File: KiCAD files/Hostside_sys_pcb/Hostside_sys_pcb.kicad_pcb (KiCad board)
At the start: 2 copper layers, 45.7 x 78.7 mm, 8 parts, among them U1 L7805, U2 Raspberry Pi Pico

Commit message: host side kicad files added and updated
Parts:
- U2: value Raspberry Pi Pico -> Pico
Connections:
- BT1 pad 2: /GND -> GND
- C1 pad 2: /GND -> GND
- C2 pad 2: /GND -> GND
- MPU6050 pad 2: /GND_MPU -> GND
- RF433Tx1 pad 1: /GND -> GND
- U1 pad 2: /GND -> GND
- U2 pad 16: unconnected-(U2-Pad16) -> /SDA
- U2 pad 17: unconnected-(U2-Pad17) -> /SCL
- U2 pad 26: /SDA -> unconnected-(U2-Pad26)
- U2 pad 27: /SCL -> unconnected-(U2-Pad27)
- U2 pad 28: /GND -> GND
- U2 pad 38: /GND_MPU -> GND
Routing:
- net /SCL: track 36.8 -> 22.3 mm
- net /SDA: track 42.2 -> 29.9 mm
- net /Data: track 21.2 -> 14.3 mm
- net /GND_MPU: track 6.28 -> 0.00 mm
- net /VCC_3.3: track 53.9 -> 58.3 mm
- net /GND: track 3.83 -> 0.00 mm
- added copper zone on B.Cu, net GND
- removed copper zone on B.Cu, net /GND

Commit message: Hostside kicad files updated and added
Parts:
- C1, C2: footprint Capacitor_THT:CP_Radial_D5.0mm_P2.00mm -> Capacitor_THT:CP_Radial_D5.0mm_P2.50mm
- D1: footprint Diode_THT:D_A-405_P7.62mm_Horizontal -> Diode_THT:D_A-405_P2.54mm_Vertical_KathodeUp
- moved D1 3.13 mm to (95.2, 52.1)
- moved MPU6050 1.60 mm to (64.9, 107.1)
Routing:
- net Net-(D1-Pad1): track 9.52 -> 11.8 mm
- net /SDA: track 29.9 -> 31.7 mm
- net /VCC_3.3: track 58.3 -> 56.8 mm
- net /Vin_5V: track 64.7 -> 66.1 mm
- net /SCL: track 22.3 -> 23.5 mm

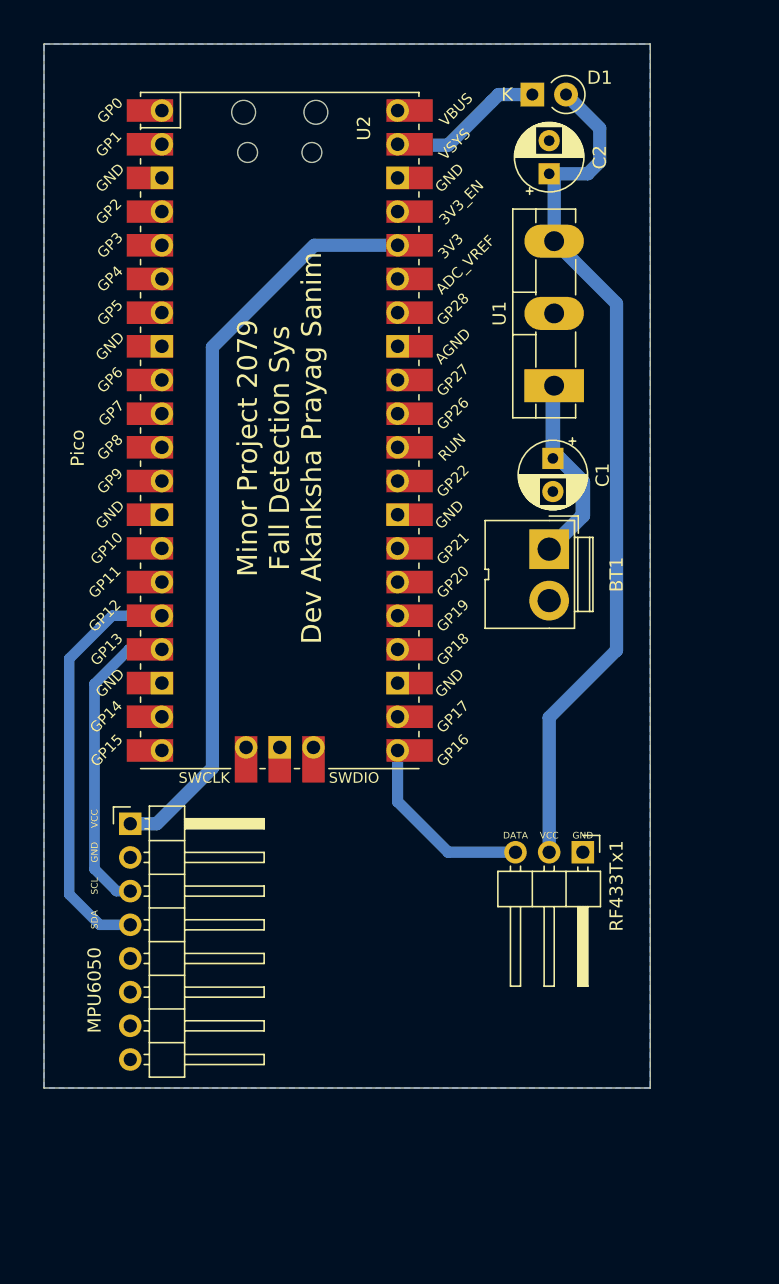
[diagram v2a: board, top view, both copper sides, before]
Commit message: clearance updated in hostside pcb
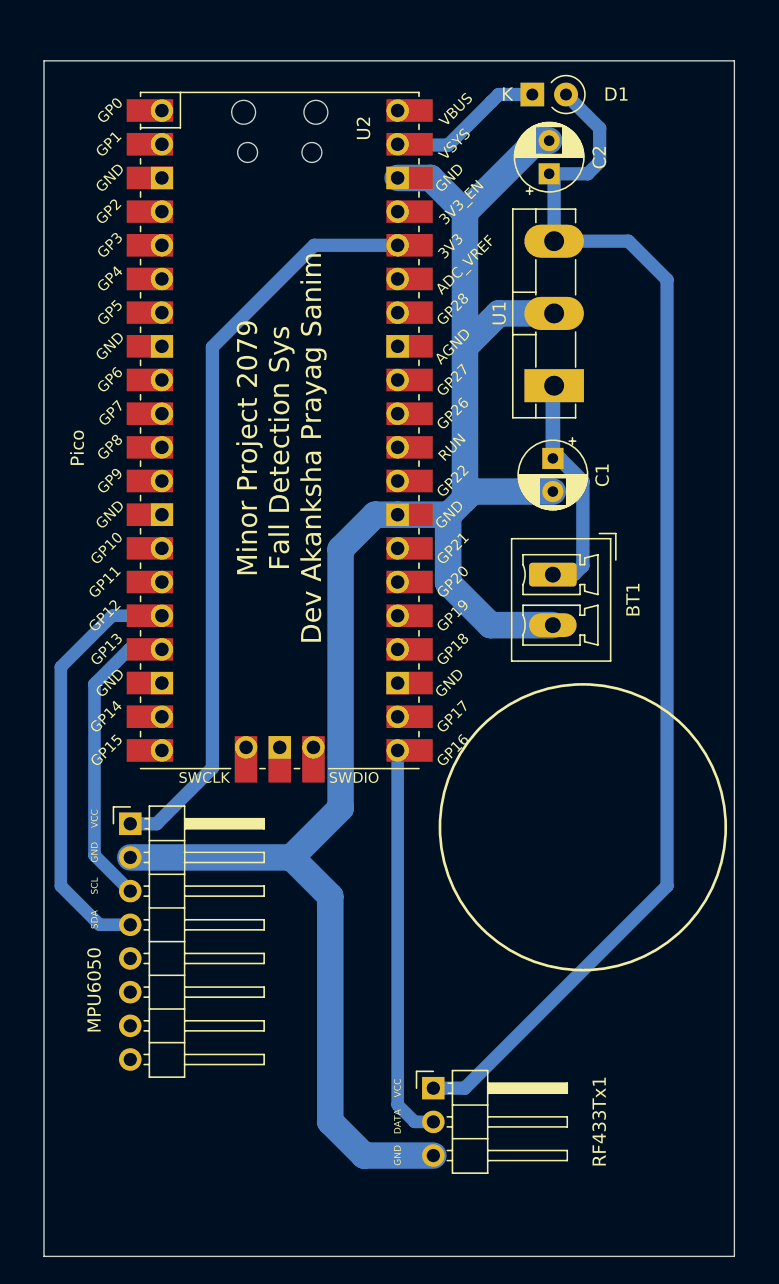
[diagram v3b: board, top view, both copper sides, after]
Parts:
- BT1: footprint Connector:JWT_A3963_1x02_P3.96mm_Vertical -> Connector_Phoenix_MC:PhoenixContact_MCV_1,5_2-G-3.81_1x02_P3.81mm_Vertical
- moved RF433Tx1 21.1 mm to (87.8, 127.0), turned to 0 degrees
- moved BT1 1.94 mm to (96.8, 88.3)
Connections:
- RF433Tx1 pad 1: GND -> /Vin_5V
- RF433Tx1 pad 2: /Vin_5V -> /Data
- RF433Tx1 pad 3: /Data -> GND
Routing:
- net GND: track 0.00 -> 143.2 mm
- net /Vin_5V: track 66.1 -> 95.3 mm
- net /Data: track 14.3 -> 30.0 mm
- net Net-(BT1-Pad1): track 14.6 -> 17.4 mm
- net /SCL: track 23.5 -> 22.9 mm
- net /SDA: track 31.7 -> 32.2 mm
- removed copper zone on B.Cu, net GND
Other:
- board size 45.7 x 78.7 mm -> 52.1 x 90.2 mm

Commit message: Use case and Sequence diagram added
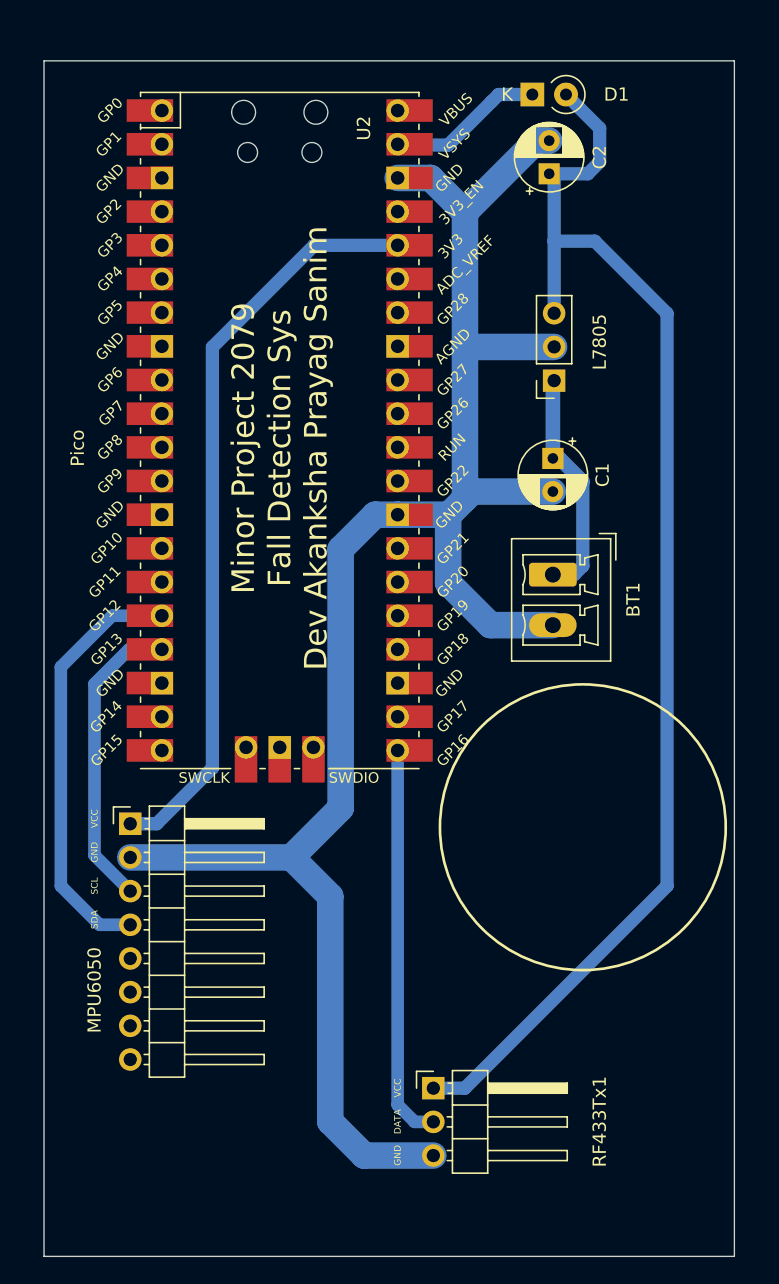
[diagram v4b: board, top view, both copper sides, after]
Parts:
- U1: footprint Package_TO_SOT_THT:TO-3P-3_Vertical -> Connector_PinSocket_2.54mm:PinSocket_1x03_P2.54mm_Vertical
- moved U1 0.39 mm to (96.9, 73.6), turned to 180 degrees
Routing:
- net /Vin_5V: track 95.3 -> 99.3 mm
- net GND: track 143.2 -> 142.1 mm
- net Net-(BT1-Pad1): track 17.4 -> 17.9 mm

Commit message: Host side pcb updates
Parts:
- removed RF433Tx1: Conn_01x03_Female, Connector_PinHeader_2.54mm:PinHeader_1x03_P2.54mm_Horizontal
- added HC-05 Bluetooth: Conn_01x06_Female, Connector_PinHeader_2.54mm:PinHeader_1x06_P2.54mm_Vertical, F.Cu at (87.9, 128.3)
- moved C2 3.20 mm to (97.8, 61.0)
- moved D1 1.32 mm to (95.6, 53.3)
- renumbered U2 to U1, U1 to U2
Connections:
- U1 pad 21: /Data -> /tx
- U1 pad 22: unconnected-(U2-Pad22) -> /rx
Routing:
- net /Data: track 30.0 -> 0.00 mm
- net /rx: track 0.00 -> 27.9 mm
- net /tx: track 0.00 -> 18.7 mm
- net GND: track 142.1 -> 131.7 mm
- net /SCL: track 22.9 -> 23.6 mm
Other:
- board size 52.1 x 90.2 mm -> 53.3 x 81.3 mm
- board text added: "+"
- board text added: "-"
- board text added: "C1:C2=1:10"
- board text added: "EN"
- board text added: "MPU6050"
- board text added: "RX"
- board text added: "TX"
- board text removed: "DATA"

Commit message: files merge
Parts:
- moved HC-05 Bluetooth 6.42 mm to (88.9, 134.6)
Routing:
- net GND: track 131.7 -> 139.0 mm
- net /rx: track 27.9 -> 33.9 mm
- net /tx: track 18.7 -> 24.5 mm
- net /Vin_5V: track 98.8 -> 104.2 mm
- net (no net): vias 0 -> 6
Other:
- board size 53.3 x 81.3 mm -> 53.3 x 92.7 mm
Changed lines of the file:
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@@
   )
   (footprint "Connector_PinHeader_2.54mm:PinHeader_1x06_P2.54mm_Vertical" (layer "F.Cu")
-    (at 87.9475 128.27 180)
+    (at 88.9 134.62 180)
     (descr "Through hole straight pin header, 1x06, 2.54mm pitch, single row")
     (tags "Through hole pin header THT 1x06 2.54mm single row")
@@
   (gr_poly
     (pts
-      (xy 110.49 130.81)
-      (xy 57.15 130.81)
-      (xy 57.15 49.53)
-      (xy 110.49 49.53)
+      (xy 110.49 139.7)
+      (xy 57.15 139.7)
+      (xy 57.15 46.99)
+      (xy 110.49 46.99)
     ) (layer "Edge.Cuts") (width 0.1) (fill none))
   (gr_text "MPU6050" (at 76.2 115.57 90) (layer "F.SilkS")
@@
     (effects (font (size 0.5 0.5) (thickness 0.125)))
   )
-  (gr_text "VCC\n" (at 85.09 125.73 90) (layer "F.SilkS")
-    (effects (font (size 0.5 0.5) (thickness 0.125)))
-  )
-  (gr_text "TX" (at 85.09 120.65 90) (layer "F.SilkS")
+  (gr_text "VCC\n" (at 86.0425 130.81 90) (layer "F.SilkS")
+    (effects (font (size 0.5 0.5) (thickness 0.125)))
+  )
+  (gr_text "TX" (at 86.0425 125.73 90) (layer "F.SilkS")
     (effects (font (size 0.5 0.5) (thickness 0.125)))
   )
@@
     (effects (font (size 0.5 0.5) (thickness 0.125)))
   )
-  (gr_text "RX" (at 85.09 118.11 90) (layer "F.SilkS")
-    (effects (font (size 0.5 0.5) (thickness 0.125)))
-  )
-  (gr_text "GND" (at 85.09 123.19 90) (layer "F.SilkS")
+  (gr_text "RX" (at 86.0425 123.19 90) (layer "F.SilkS")
+    (effects (font (size 0.5 0.5) (thickness 0.125)))
+  )
+  (gr_text "GND" (at 86.0425 128.27 90) (layer "F.SilkS")
     (effects (font (size 0.5 0.5) (thickness 0.125)))
   )
@@
     (effects (font (size 1.5 1.5) (thickness 0.375)))
   )
-  (gr_text "EN" (at 85.09 128.27 90) (layer "F.SilkS")
-    (effects (font (size 0.5 0.5) (thickness 0.125)))
-  )
+  (gr_text "EN" (at 86.0425 133.35 90) (layer "F.SilkS")
+    (effects (font (size 0.5 0.5) (thickness 0.125)))
+  )
+  (dimension (type aligned) (layer "B.Cu")
+    (pts (xy 57.15 144.78) (xy 110.49 144.78))
+    (height 1.27)
+    (gr_text "53.3400 mm" (at 83.82 144.25) (layer "B.Cu")
+      (effects (font (size 1.5 1.5) (thickness 0.3)))
+    )
+    (format (units 3) (units_format 1) (precision 4))
+    (style (thickness 0.2) (arrow_length 1.27) (text_position_mode 0) (extension_height 0.58642) (extension_offset 0.5) keep_text_aligned)
+  )
+  (dimension (type aligned) (layer "B.Cu")
+    (pts (xy 127 46.99) (xy 127 139.7))
+    (height 2.54)
+    (gr_text "92.7100 mm" (at 122.66 93.345 90) (layer "B.Cu")
+      (effects (font (size 1.5 1.5) (thickness 0.3)))
+    )
+    (format (units 3) (units_format 1) (precision 4))
+    (style (thickness 0.2) (arrow_length 1.27) (text_position_mode 0) (extension_height 0.58642) (extension_offset 0.5) keep_text_aligned)
+  )
+  (via (at 106.68 137.16) (size 2) (drill 1) (layers "F.Cu" "B.Cu") (free) (net 0))
+  (via (at 60.96 137.16) (size 2) (drill 1) (layers "F.Cu" "B.Cu") (free) (net 0))
+  (via (at 106.68 49.53) (size 2) (drill 1) (layers "F.Cu" "B.Cu") (free) (net 0))
+  (via (at 105.41 118.11) (size 1.5) (drill 1) (layers "F.Cu" "B.Cu") (free) (net 0))
+  (via (at 60.96 49.53) (size 2) (drill 1) (layers "F.Cu" "B.Cu") (free) (net 0))
+  (via (at 91.44 96.52) (size 1.5) (drill 1) (layers "F.Cu" "B.Cu") (remove_unused_layers) (keep_end_layers) (free) (net 0))
   (segment (start 97.29479 79.51479) (end 96.7995 79.51479) (width 1.1) (layer "B.Cu") (net 1))
   (segment (start 99.06 81.28) (end 97.29479 79.51479) (width 1.1) (layer "B.Cu") (net 1))
@@
   (segment (start 90.17 71.12) (end 90.17 82.55) (width 2) (layer "B.Cu") (net 2))
   (segment (start 90.17 71.12) (end 90.17 60.96) (width 2) (layer "B.Cu") (net 2))
+  (segment (start 77.08 109.61) (end 77.08 121.53) (width 2) (layer "B.Cu") (net 2))
   (segment (start 83.82 83.76) (end 85.09 83.76) (width 2) (layer "B.Cu") (net 2))
   (segment (start 96.7975 92.09) (end 92.09 92.09) (width 2) (layer "B.Cu") (net 2))
-  (segment (start 85.09 123.19) (end 87.9475 123.19) (width 2) (layer "B.Cu") (net 2))
   (segment (start 80.79 105.9) (end 80.79 86.79) (width 2) (layer "B.Cu") (net 2))
+  (segment (start 77.08 121.53) (end 85.09 129.54) (width 2) (layer "B.Cu") (net 2))
   (segment (start 87.57 58.36) (end 85.09 58.36) (width 2) (layer "B.Cu") (net 2))
-  (segment (start 77.08 109.61) (end 77.08 115.18) (width 2) (layer "B.Cu") (net 2))
   (segment (start 92.65 58.48) (end 97.79 58.48) (width 2) (layer "B.Cu") (net 2))
+  (segment (start 85.09 129.54) (end 88.9 129.54) (width 2) (layer "B.Cu") (net 2))
   (segment (start 90.17 82.55) (end 88.9 83.82) (width 2) (layer "B.Cu") (net 2))
   (segment (start 88.9 88.9) (end 88.9 83.82) (width 2) (layer "B.Cu") (net 2))
@@
   (segment (start 90.70521 82.01479) (end 90.17 82.55) (width 2) (layer "B.Cu") (net 2))
   (segment (start 96.7995 82.01479) (end 90.70521 82.01479) (width 2) (layer "B.Cu") (net 2))
-  (segment (start 77.08 115.18) (end 85.09 123.19) (width 2) (layer "B.Cu") (net 2))
   (segment (start 90.17 60.96) (end 92.65 58.48) (width 2) (layer "B.Cu") (net 2))
-  (segment (start 105.41 71.12) (end 99.435 65.145) (width 1) (layer "B.Cu") (net 3))
-  (segment (start 91.44 125.73) (end 105.41 111.76) (width 0.95) (layer "B.Cu") (net 3))
-  (segment (start 87.9475 125.73) (end 91.44 125.73) (width 0.95) (layer "B.Cu") (net 3))
+  (segment (start 91.44 132.08) (end 93.98 129.54) (width 1) (layer "B.Cu") (net 3))
+  (segment (start 88.9 132.08) (end 91.44 132.08) (width 1) (layer "B.Cu") (net 3))
   (segment (start 101.6 53.34) (end 98.14 53.34) (width 1) (layer "B.Cu") (net 3))
   (segment (start 102.87 59.69) (end 102.87 54.61) (width 1) (layer "B.Cu") (net 3))
+  (segment (start 105.41 111.76) (end 105.41 71.12) (width 1) (layer "B.Cu") (net 3))
   (segment (start 102.87 54.61) (end 101.6 53.34) (width 1) (layer "B.Cu") (net 3))
+  (segment (start 93.98 129.54) (end 93.98 123.19) (width 1) (layer "B.Cu") (net 3))
+  (segment (start 93.98 123.19) (end 105.41 111.76) (width 1) (layer "B.Cu") (net 3))
   (segment (start 97.79 60.98) (end 101.58 60.98) (width 1) (layer "B.Cu") (net 3))
+  (segment (start 99.435 65.145) (end 96.895 65.145) (width 1) (layer "B.Cu") (net 3))
   (segment (start 96.895 61.875) (end 97.79 60.98) (width 1) (layer "B.Cu") (net 3))
-  (segment (start 99.435 65.145) (end 96.895 65.145) (width 1) (layer "B.Cu") (net 3))
   (segment (start 96.895 68.565) (end 96.895 65.145) (width 1) (layer "B.Cu") (net 3))
   (segment (start 101.58 60.98) (end 102.87 59.69) (width 1) (layer "B.Cu") (net 3))
-  (segment (start 105.41 111.76) (end 105.41 71.12) (width 1) (layer "B.Cu") (net 3))
+  (segment (start 105.41 71.12) (end 99.435 65.145) (width 1) (layer "B.Cu") (net 3))
   (segment (start 96.895 65.145) (end 96.895 61.875) (width 1) (layer "B.Cu") (net 3))
   (segment (start 90.17 55.88) (end 85.15 55.88) (width 1) (layer "B.Cu") (net 4))
@@
   (segment (start 63.56 91.38) (end 67.31 91.38) (width 0.95) (layer "B.Cu") (net 7))
   (segment (start 64.925 114.69) (end 62.62 114.69) (width 0.95) (layer "B.Cu") (net 7))
+  (segment (start 88.9 127) (end 91.44 124.46) (width 1) (layer "B.Cu") (net 9))
   (segment (start 91.44 117.1575) (end 91.44 101.6) (width 0.95) (layer "B.Cu") (net 9))
-  (segment (start 87.9475 120.65) (end 91.44 117.1575) (width 0.95) (layer "B.Cu") (net 9))
+  (segment (start 91.44 124.46) (end 91.44 117.1575) (width 1) (layer "B.Cu") (net 9))
   (segment (start 91.44 101.6) (end 88.84 99) (width 0.95) (layer "B.Cu") (net 9))
   (segment (start 88.84 99) (end 85.09 99) (width 0.95) (layer "B.Cu") (net 9))
-  (segment (start 86.36 118.11) (end 85.09 116.84) (width 0.95) (layer "B.Cu") (net 10))
-  (segment (start 87.9475 118.11) (end 86.36 118.11) (width 0.95) (layer "B.Cu") (net 10))
+  (segment (start 85.09 120.65) (end 85.09 116.84) (width 1) (layer "B.Cu") (net 10))
+  (segment (start 88.9 124.46) (end 85.09 120.65) (width 1) (layer "B.Cu") (net 10))
   (segment (start 85.09 116.84) (end 85.09 101.54) (width 0.95) (layer "B.Cu") (net 10))
 )
